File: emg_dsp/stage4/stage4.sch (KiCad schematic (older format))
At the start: 174 parts, among them U1 TPS71733, U10 TPS62410, U11 FCI_USB_B, U12 VDD_3.35, U13 VCC_1.2, U14 VAA_2.0, U15 EN_VCC, U16 VAA_VDD, U17 VDD_2.85/3.35, U18 VDD_2.7, U19 TPS71727, U2 ADM3202, U20 CLKOUT, U21 ABM10XTAL, U22 BF532-160, U23 TSCLK0, U24 NRF24L01, U25 AT45DB081D, U26 74LCX541, U27 MAX6711Z, U28 TESTCON, U29 ANTENNA, U3 MAX3421E, U30 74LCX541, U31 74LCX541, U4 GND, U5 VEE, U6 ADSP_JTAG_CON, U7 NX3225SA, U8 FAN2001, U9 RS232_CON

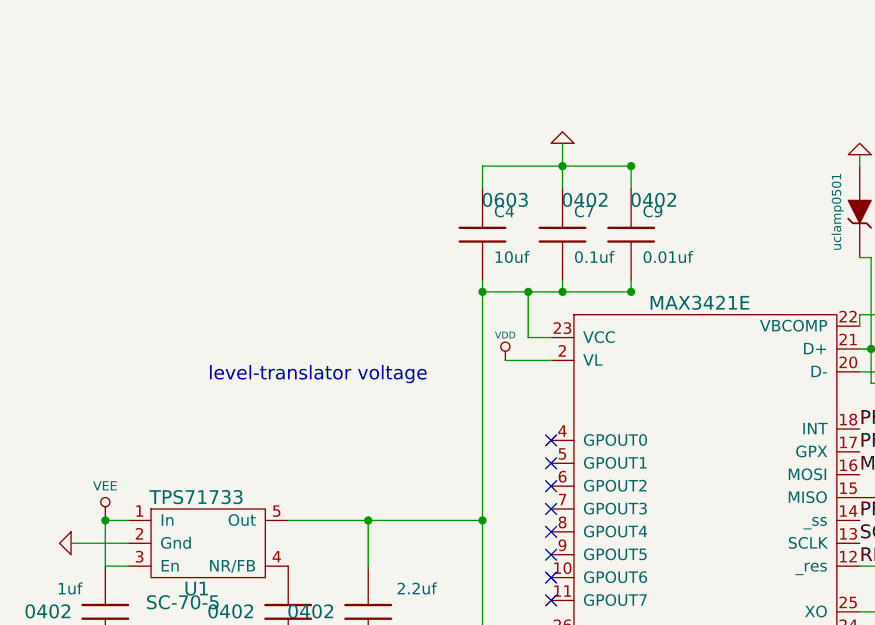
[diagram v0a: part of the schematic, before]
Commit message: removed some extraneous jumpers; going to start on zones / power planes soon, I hope.
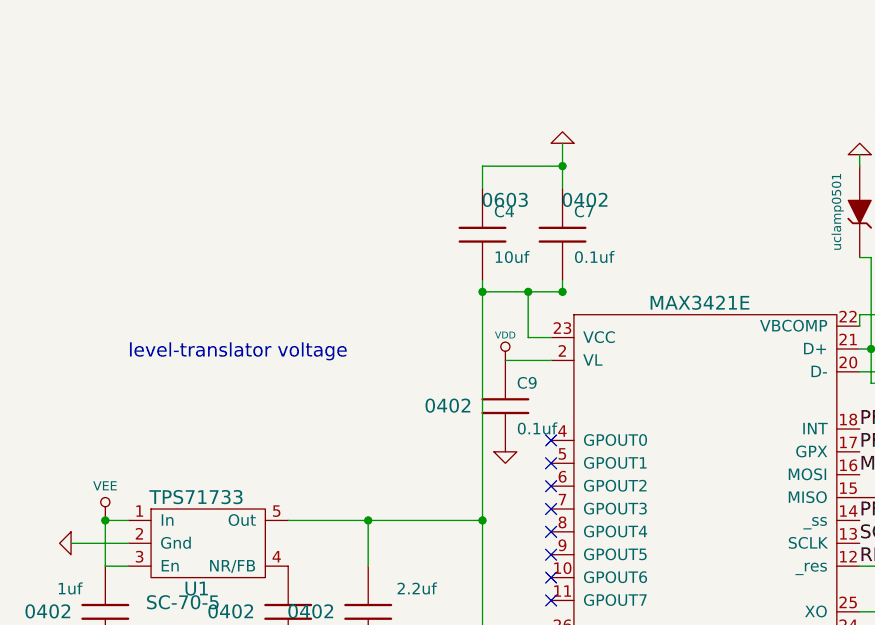
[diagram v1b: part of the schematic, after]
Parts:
- C9: value 0.01uf -> 0.1uf
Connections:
- net GND: now also C9.2; no longer C9.1
- net VDD: now also C9.1
- net at C17.2, C3.2, C4.2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: no longer C9.2
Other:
- moved on the sheet: C9
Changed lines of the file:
@@
-EESchema Schematic File Version 2  date Tue 16 Feb 2010 05:30:46 PM EST
+EESchema Schematic File Version 2  date Tue 16 Feb 2010 06:01:42 PM EST
 LIBS:power,device,emg_sym,/home/tlh24/svn/myopen/emg_dsp/lib/linear,./stage4.cache
 EELAYER 24  0
@@
 $EndDescr
 $Comp
-L GND #PWR01
-U 1 1 4B7AE9CB
-P 16450 2650
-F 0 "#PWR01" H 16450 2650 30  0001 C CNN
-F 1 "GND" H 16450 2580 30  0001 C CNN
-	1    16450 2650
-	1    0    0    -1
-$EndComp
-$Comp
-L VDD #PWR02
-U 1 1 4B7AE9CA
-P 16450 2250
-F 0 "#PWR02" H 16450 2350 30  0001 C CNN
-F 1 "VDD" H 16450 2360 30  0000 C CNN
-	1    16450 2250
-	1    0    0    -1
-$EndComp
-$Comp
-L C C359
-U 1 1 4B7AE9C9
-P 16450 2450
-F 0 "C359" H 16500 2550 50  0000 L CNN
-F 1 "0.1uf" H 16500 2350 50  0000 L CNN
-F 2 "0402" H 16550 2600 60  0000 C CNN
-	1    16450 2450
-	1    0    0    -1
-$EndComp
-$Comp
-L GND #PWR03
-U 1 1 4B7AE9C6
-P 16450 5000
-F 0 "#PWR03" H 16450 5000 30  0001 C CNN
-F 1 "GND" H 16450 4930 30  0001 C CNN
-	1    16450 5000
-	1    0    0    -1
-$EndComp
-$Comp
-L VDD #PWR04
-U 1 1 4B7AE9C5
-P 16450 4600
-F 0 "#PWR04" H 16450 4700 30  0001 C CNN
-F 1 "VDD" H 16450 4710 30  0000 C CNN
-	1    16450 4600
-	1    0    0    -1
-$EndComp
-$Comp
-L C C360
-U 1 1 4B7AE9C4
-P 16450 4800
-F 0 "C360" H 16500 4900 50  0000 L CNN
-F 1 "0.1uf" H 16500 4700 50  0000 L CNN
-F 2 "0402" H 16550 4950 60  0000 C CNN
-	1    16450 4800
-	1    0    0    -1
-$EndComp
-$Comp
-L GND #PWR05
-U 1 1 4B797342
-P 13950 4750
-F 0 "#PWR05" H 13950 4750 30  0001 C CNN
-F 1 "GND" H 13950 4680 30  0001 C CNN
-	1    13950 4750
-	1    0    0    -1
-$EndComp
-$Comp
-L VDD #PWR06
-U 1 1 4B79733D
-P 13950 4350
-F 0 "#PWR06" H 13950 4450 30  0001 C CNN
-F 1 "VDD" H 13950 4460 30  0000 C CNN
-	1    13950 4350
-	1    0    0    -1
-$EndComp
-$Comp
-L C C357
-U 1 1 4B797335
-P 13950 4550
-F 0 "C357" H 14000 4650 50  0000 L CNN
-F 1 "0.1uf" H 14000 4450 50  0000 L CNN
-F 2 "0402" H 14050 4700 60  0000 C CNN
-	1    13950 4550
-	1    0    0    -1
-$EndComp
-Text Notes 4150 1150 0    60   ~ 0
-I hope this is enough!
+L GND #PWR?
+U 1 1 4B7B23B8
+P 650 2850
+F 0 "#PWR?" H 650 2850 30  0001 C CNN
+F 1 "GND" H 650 2780 30  0001 C CNN
+	1    650  2850
+	1    0    0    -1
+$EndComp
+Wire Wire Line
+	550  2150 900  2150
 Connection ~ 4900 1050
 Wire Wire Line
@@
 	4300 7550 4350 7550
 Wire Wire Line
-	550  1600 1200 1600
-Wire Wire Line
 	5050 5100 5300 5100
 Wire Wire Line
@@
 Wire Wire Line
 	9450 3000 8600 3000
-Connection ~ 1200 1600
 Connection ~ 1550 8750
 Wire Wire Line
@@
 Connection ~ 900  1600
 Connection ~ 750  2150
-Wire Wire Line
-	1200 2100 1200 2150
 Wire Wire Line
 	7900 2600 7900 2700
@@
 Connection ~ 900  2150
 Wire Wire Line
-	550  1600 550  1700
-Wire Wire Line
-	1200 1600 1200 1700
+	550  1700 550  1600
 Wire Wire Line
 	900  1700 900  1500
@@
 Wire Wire Line
 	850  2350 750  2350
-Connection ~ 1200 2150
 Wire Wire Line
 	650  2450 850  2450
-Wire Wire Line
-	1200 2150 550  2150
 Wire Wire Line
 	4750 9950 4850 9950
@@
 Wire Wire Line
 	4050 1050 5650 1050
+Wire Wire Line
+	550  1600 900  1600
+$Comp
+L GND #PWR01
+U 1 1 4B7AE9CB
+P 16450 2650
+F 0 "#PWR01" H 16450 2650 30  0001 C CNN
+F 1 "GND" H 16450 2580 30  0001 C CNN
+	1    16450 2650
+	1    0    0    -1
+$EndComp
+$Comp
+L VDD #PWR02
+U 1 1 4B7AE9CA
+P 16450 2250
+F 0 "#PWR02" H 16450 2350 30  0001 C CNN
+F 1 "VDD" H 16450 2360 30  0000 C CNN
+	1    16450 2250
+	1    0    0    -1
+$EndComp
+$Comp
+L C C359
+U 1 1 4B7AE9C9
+P 16450 2450
+F 0 "C359" H 16500 2550 50  0000 L CNN
+F 1 "0.1uf" H 16500 2350 50  0000 L CNN
+F 2 "0402" H 16550 2600 60  0000 C CNN
+	1    16450 2450
+	1    0    0    -1
+$EndComp
+$Comp
+L GND #PWR03
+U 1 1 4B7AE9C6
+P 16450 5000
+F 0 "#PWR03" H 16450 5000 30  0001 C CNN
+F 1 "GND" H 16450 4930 30  0001 C CNN
+	1    16450 5000
+	1    0    0    -1
+$EndComp
+$Comp
+L VDD #PWR04
+U 1 1 4B7AE9C5
+P 16450 4600
+F 0 "#PWR04" H 16450 4700 30  0001 C CNN
+F 1 "VDD" H 16450 4710 30  0000 C CNN
+	1    16450 4600
+	1    0    0    -1
+$EndComp
+$Comp
+L C C360
+U 1 1 4B7AE9C4
+P 16450 4800
+F 0 "C360" H 16500 4900 50  0000 L CNN
+F 1 "0.1uf" H 16500 4700 50  0000 L CNN
+F 2 "0402" H 16550 4950 60  0000 C CNN
+	1    16450 4800
+	1    0    0    -1
+$EndComp
+$Comp
+L GND #PWR05
+U 1 1 4B797342
+P 13950 4750
+F 0 "#PWR05" H 13950 4750 30  0001 C CNN
+F 1 "GND" H 13950 4680 30  0001 C CNN
+	1    13950 4750
+	1    0    0    -1
+$EndComp
+$Comp
+L VDD #PWR06
+U 1 1 4B79733D
+P 13950 4350
+F 0 "#PWR06" H 13950 4450 30  0001 C CNN
+F 1 "VDD" H 13950 4460 30  0000 C CNN
+	1    13950 4350
+	1    0    0    -1
+$EndComp
+$Comp
+L C C357
+U 1 1 4B797335
+P 13950 4550
+F 0 "C357" H 14000 4650 50  0000 L CNN
+F 1 "0.1uf" H 14000 4450 50  0000 L CNN
+F 2 "0402" H 14050 4700 60  0000 C CNN
+	1    13950 4550
+	1    0    0    -1
+$EndComp
+Text Notes 4150 1150 0    60   ~ 0
+I hope this is enough!
 $Comp
 L GND #PWR07
@@
 Text Notes 11800 1800 0    60   ~ 0
 use the 2.7V version
-Text Notes -650 2550 0    60   ~ 0
+Text Notes -1000 2450 0    60   ~ 0
 level-translator voltage
 $Comp
@@
 L C C9
 U 1 1 49068A61
-P 1200 1900
-F 0 "C9" H 1250 2000 50  0000 L CNN
-F 1 "0.01uf" H 1250 1800 50  0000 L CNN
-F 2 "0402" H 1300 2050 60  0000 C CNN
-	1    1200 1900
-	1    0    0    -1
-$EndComp
+P 650 2650
+F 0 "C9" H 700 2750 50  0000 L CNN
+F 1 "0.1uf" H 700 2550 50  0000 L CNN
+F 2 "0402" H 400 2650 60  0000 C CNN
+	1    650  2650
+	1    0    0    -1
+$EndComp

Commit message: still need to place some components, do the power nets, figure out how I'm going to get Vaa/Vcc/Vdd to the blackfin ...
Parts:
- removed U4: GND, 2x100mil, symbol JUMP
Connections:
- net VEE: now also U5.2

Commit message: cleaned up the power supplies.  not sure what i was thinking before - 2.85V should be fine for Vdd.
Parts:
- removed C33: 1uf, 0402, symbol C
- removed C35: 0.01uf, 0402, symbol C
- removed C37: 2.2uf, 0402, symbol C
- removed R9: 1M, 0402, symbol R
- removed U12: VDD_3.35, 2x100mil, symbol JUMP
- removed U18: VDD_2.7, 2x100mil, symbol JUMP
- removed U19: TPS71727, SC-70-5, symbol TPS717
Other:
- note added: "2.85V"
- note added: "so 2.85V inputs should be ok"
- note removed: "2.7, 2.85, or 3.35V"
- note removed: "DNP unless Vdd = 2.7V"
- note removed: "drives the LMVs and radio"
- note removed: "increase Vdd to 3.35V"
- note removed: "needed for stim"
- note removed: "so 2.7V inputs should be ok"

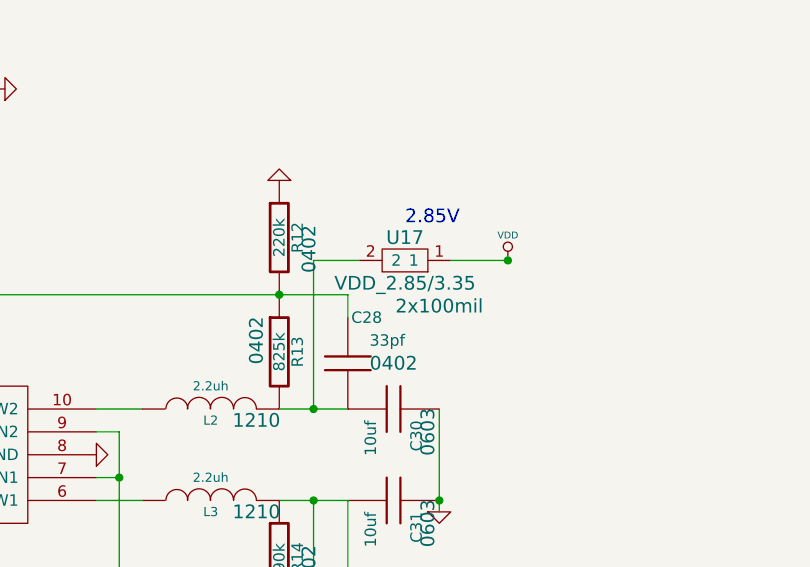
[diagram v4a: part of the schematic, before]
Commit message: changed the meg isolator to something that will work at 2.7V
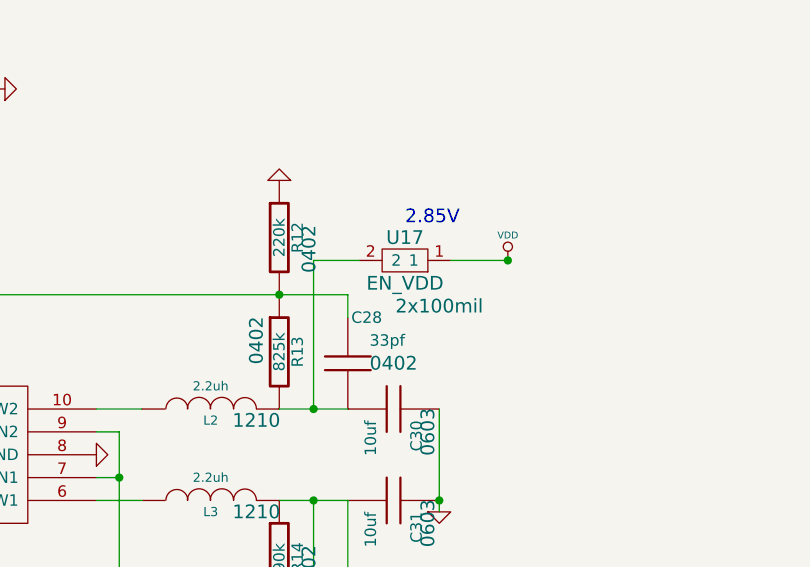
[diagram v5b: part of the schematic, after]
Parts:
- U17: value VDD_2.85/3.35 -> EN_VDD

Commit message: ?
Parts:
- removed U23: TSCLK0, 2x100mil, symbol JUMP
- added R274: 25, 0402, symbol R
- added TP177: G, TP, symbol TP
- added TP178: TSCLK0, TP, symbol TP
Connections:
- net GND: now also TP177.1; no longer U5.1
- net TSCLK0: now also R274.1, TP178.1
- net VEE: now also U5.1; no longer C11.2, C12.2, C15.2, C18.2, C8.2, U10.3 (VIN), U10.7 (EN1), U10.9 (EN2), U5.2, U8.1 (Vin), U8.3 (EN)
- net at U22.C9 (PPI_CLK): now also R274.2
- new net: C11.2, C12.2, C15.2, C18.2, C8.2, U10.3 (VIN), U10.7 (EN1), U10.9 (EN2), U5.2, U8.1 (Vin), U8.3 (EN)

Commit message: layout 95% done ...
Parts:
- removed TP178: TSCLK0, TP, symbol TP

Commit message: it's zone time~!
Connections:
- net GND: now also U9.g1 (g), U9.g2 (g)
